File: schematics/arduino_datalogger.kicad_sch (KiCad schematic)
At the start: 9 parts, among them J1 SD card module, J2 RTC module, SW1 SW_Push, U1 DHT22

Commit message: Algunos cambios esquema
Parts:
- added J3: Screw_Terminal_01x03, TerminalBlock:TerminalBlock_bornier-3_P5.08mm, symbol Connector:Screw_Terminal_01x03
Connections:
- net +5V: now also J3.1 (Pin_1)
- net GND: now also J3.3 (Pin_3)
- net DHTDATA: now reaches A1.19 (A0), R3.2, U1.2 (IO)
- net DHTDATA: now also J3.2 (Pin_2)
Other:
- note added: "Not on board"
- moved on the sheet: R3, U1

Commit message: Teniendo en cuenta las medidas reales de los modulos
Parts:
- removed J3: Screw_Terminal_01x03, TerminalBlock:TerminalBlock_bornier-3_P5.08mm, symbol Connector:Screw_Terminal_01x03
- added J3: DHT, Connector_PinSocket_2.54mm:PinSocket_1x06_P2.54mm_Vertical, symbol Connector:Conn_01x03_Socket
- J1, J2: footprint Connector_PinSocket_2.00mm:PinSocket_1x06_P2.00mm_Vertical -> Connector_PinSocket_2.54mm:PinSocket_1x06_P2.54mm_Vertical
- SW1: footprint Button_Switch_THT:SW_PUSH_6mm -> Button_Switch_THT:SW_PUSH-12mm
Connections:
- net +5V: now also J3.1 (Pin_1)
- net DHTDATA: now also J3.2 (Pin_2)
- net GND: now also J3.3 (Pin_3); no longer A1.4 (GND)
- no-connect marks 15 -> 16
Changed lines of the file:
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@@
     (company "Lab. Biología de los Artrópodos - FaCENA - UNNE")
-  )
-  (junction (at 93.98 85.09) (diameter 0) (color 0 0 0 0)
   )
   (junction (at 121.92 54.61) (diameter 0) (color 0 0 0 0)
@@
   (no_connect (at 50.8 57.15))
   (no_connect (at 106.68 53.34))
+  (no_connect (at 93.98 83.82))
   (no_connect (at 81.28 45.72))
   (no_connect (at 50.8 62.23))
@@
     (stroke (width 0) (type default))
   )
-  (wire (pts (xy 93.98 83.82) (xy 93.98 85.09))
-    (stroke (width 0) (type default))
-  )
   (wire (pts (xy 165.1 54.61) (xy 167.64 54.61))
     (stroke (width 0) (type default))
@@
     (stroke (width 0) (type default))
   )
-  (wire (pts (xy 96.52 85.09) (xy 93.98 85.09))
-    (stroke (width 0) (type default))
-  )
   (bus (pts (xy 72.39 60.96) (xy 72.39 63.5))
     (stroke (width 0) (type default))
@@
     (stroke (width 0) (type default))
   )
-  (wire (pts (xy 96.52 83.82) (xy 96.52 85.09))
-    (stroke (width 0) (type default))
-  )
   (wire (pts (xy 34.29 113.03) (xy 43.18 113.03))
     (stroke (width 0) (type default))
@@
   )
   (wire (pts (xy 74.93 34.29) (xy 73.66 34.29))
-    (stroke (width 0) (type default))
-  )
-  (wire (pts (xy 93.98 85.09) (xy 93.98 86.36))
     (stroke (width 0) (type default))
   )
@@
       (effects (font (size 1.27 1.27)) (justify left))
     )
-    (property "Footprint" "Connector_PinSocket_2.00mm:PinSocket_1x06_P2.00mm_Vertical" (at 172.72 46.99 0)
+    (property "Footprint" "Connector_PinSocket_2.54mm:PinSocket_1x06_P2.54mm_Vertical" (at 172.72 46.99 0)
       (effects (font (size 1.27 1.27)) hide)
     )
@@
     )
   )
-  (symbol (lib_id "power:GND") (at 93.98 86.36 0) (unit 1)
-    (in_bom yes) (on_board yes) (dnp no) (fields_autoplaced)
-    (property "Reference" "#PWR02" (at 93.98 92.71 0)
-      (effects (font (size 1.27 1.27)) hide)
-    )
-    (property "Value" "GND" (at 93.98 91.44 0)
-      (effects (font (size 1.27 1.27)))
-    )
-    (property "Footprint" "" (at 93.98 86.36 0)
-      (effects (font (size 1.27 1.27)) hide)
-    )
-    (property "Datasheet" "" (at 93.98 86.36 0)
+  (symbol (lib_id "power:GND") (at 96.52 83.82 0) (unit 1)
+    (in_bom yes) (on_board yes) (dnp no) (fields_autoplaced)
+    (property "Reference" "#PWR02" (at 96.52 90.17 0)
+      (effects (font (size 1.27 1.27)) hide)
+    )
+    (property "Value" "GND" (at 96.52 88.9 0)
+      (effects (font (size 1.27 1.27)))
+    )
+    (property "Footprint" "" (at 96.52 83.82 0)
+      (effects (font (size 1.27 1.27)) hide)
+    )
+    (property "Datasheet" "" (at 96.52 83.82 0)
       (effects (font (size 1.27 1.27)) hide)
     )
@@
     )
   )
-  (symbol (lib_id "Connector:Screw_Terminal_01x03") (at 129.54 58.42 0) (unit 1)
-    (in_bom yes) (on_board yes) (dnp no) (fields_autoplaced)
-    (property "Reference" "J3" (at 132.08 57.15 0)
-      (effects (font (size 1.27 1.27)) (justify left))
-    )
-    (property "Value" "Screw_Terminal_01x03" (at 132.08 59.69 0)
-      (effects (font (size 1.27 1.27)) (justify left))
-    )
-    (property "Footprint" "TerminalBlock:TerminalBlock_bornier-3_P5.08mm" (at 129.54 58.42 0)
+  (symbol (lib_id "Device:R") (at 40.64 33.02 0) (unit 1)
+    (in_bom yes) (on_board yes) (dnp no) (fields_autoplaced)
+    (property "Reference" "R1" (at 43.18 31.75 0)
+      (effects (font (size 1.27 1.27)) (justify left))
+    )
+    (property "Value" "1K" (at 43.18 34.29 0)
+      (effects (font (size 1.27 1.27)) (justify left))
+    )
+    (property "Footprint" "Resistor_THT:R_Axial_DIN0207_L6.3mm_D2.5mm_P7.62mm_Horizontal" (at 38.862 33.02 90)
+      (effects (font (size 1.27 1.27)) hide)
+    )
+    (property "Datasheet" "~" (at 40.64 33.02 0)
+      (effects (font (size 1.27 1.27)) hide)
+    )
+    (pin "1")
+    (pin "2")
+    (instances
+      (project "arduino_datalogger"
+        (path "/b8de69f0-971f-4260-bee1-9a12f00351ec"
+          (reference "R1") (unit 1)
+        )
+      )
+    )
+  )
+  (symbol (lib_id "Connector:Conn_01x03_Socket") (at 129.54 58.42 0) (unit 1)
+    (in_bom yes) (on_board yes) (dnp no) (fields_autoplaced)
+    (property "Reference" "J3" (at 130.81 57.15 0)
+      (effects (font (size 1.27 1.27)) (justify left))
+    )
+    (property "Value" "DHT" (at 130.81 59.69 0)
+      (effects (font (size 1.27 1.27)) (justify left))
+    )
+    (property "Footprint" "Connector_PinSocket_2.54mm:PinSocket_1x06_P2.54mm_Vertical" (at 129.54 58.42 0)
       (effects (font (size 1.27 1.27)) hide)
     )
@@
         (path "/b8de69f0-971f-4260-bee1-9a12f00351ec"
           (reference "J3") (unit 1)
-        )
-      )
-    )
-  )
-  (symbol (lib_id "Device:R") (at 40.64 33.02 0) (unit 1)
-    (in_bom yes) (on_board yes) (dnp no) (fields_autoplaced)
-    (property "Reference" "R1" (at 43.18 31.75 0)
-      (effects (font (size 1.27 1.27)) (justify left))
-    )
-    (property "Value" "1K" (at 43.18 34.29 0)
-      (effects (font (size 1.27 1.27)) (justify left))
-    )
-    (property "Footprint" "Resistor_THT:R_Axial_DIN0207_L6.3mm_D2.5mm_P7.62mm_Horizontal" (at 38.862 33.02 90)
-      (effects (font (size 1.27 1.27)) hide)
-    )
-    (property "Datasheet" "~" (at 40.64 33.02 0)
-      (effects (font (size 1.27 1.27)) hide)
-    )
-    (pin "1")
-    (pin "2")
-    (instances
-      (project "arduino_datalogger"
-        (path "/b8de69f0-971f-4260-bee1-9a12f00351ec"
-          (reference "R1") (unit 1)
         )
       )
@@
       (effects (font (size 1.27 1.27)))
     )
-    (property "Footprint" "Button_Switch_THT:SW_PUSH_6mm" (at 68.58 29.21 0)
+    (property "Footprint" "Button_Switch_THT:SW_PUSH-12mm" (at 68.58 29.21 0)
       (effects (font (size 1.27 1.27)) hide)
     )
@@
       (effects (font (size 1.27 1.27)) (justify left))
     )
-    (property "Footprint" "Connector_PinSocket_2.00mm:PinSocket_1x06_P2.00mm_Vertical" (at 172.72 66.04 0)
-      (effects (font (size 1.27 1.27)) hide)
-    )
+    (property "Footprint" "Connector_PinSocket_2.54mm:PinSocket_1x06_P2.54mm_Vertical" (at 172.72 66.04 0)
+      (effects (font (size 1.27 1.27)) hide)
+    )

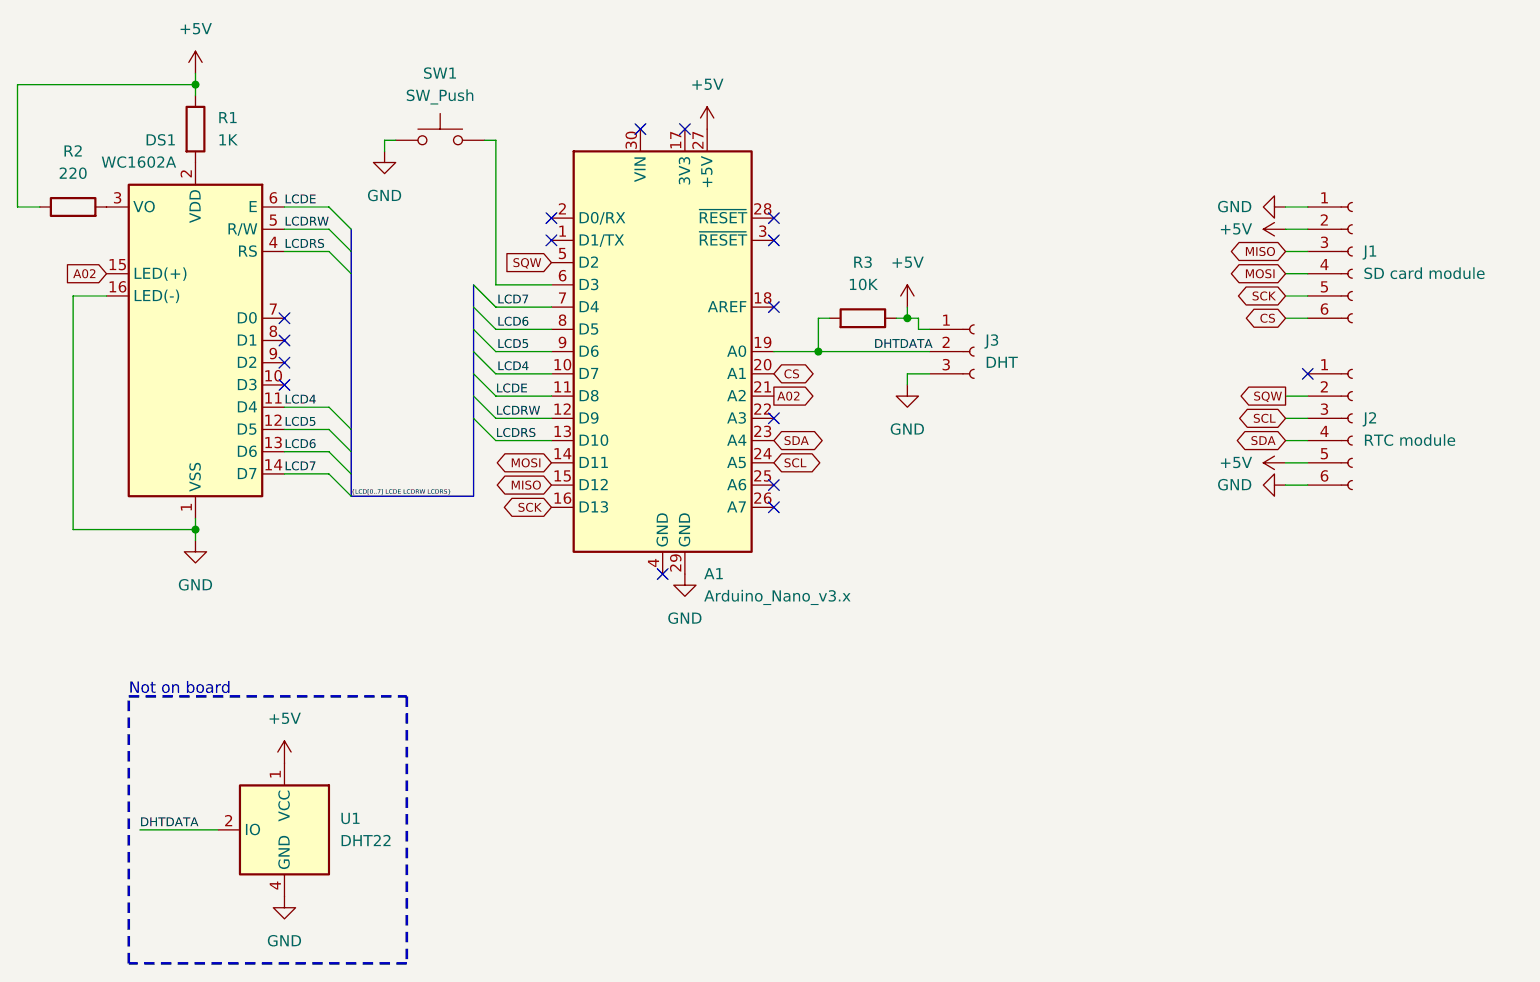
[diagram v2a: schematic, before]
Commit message: Simbolos y footprints para modulo RTC y microSD
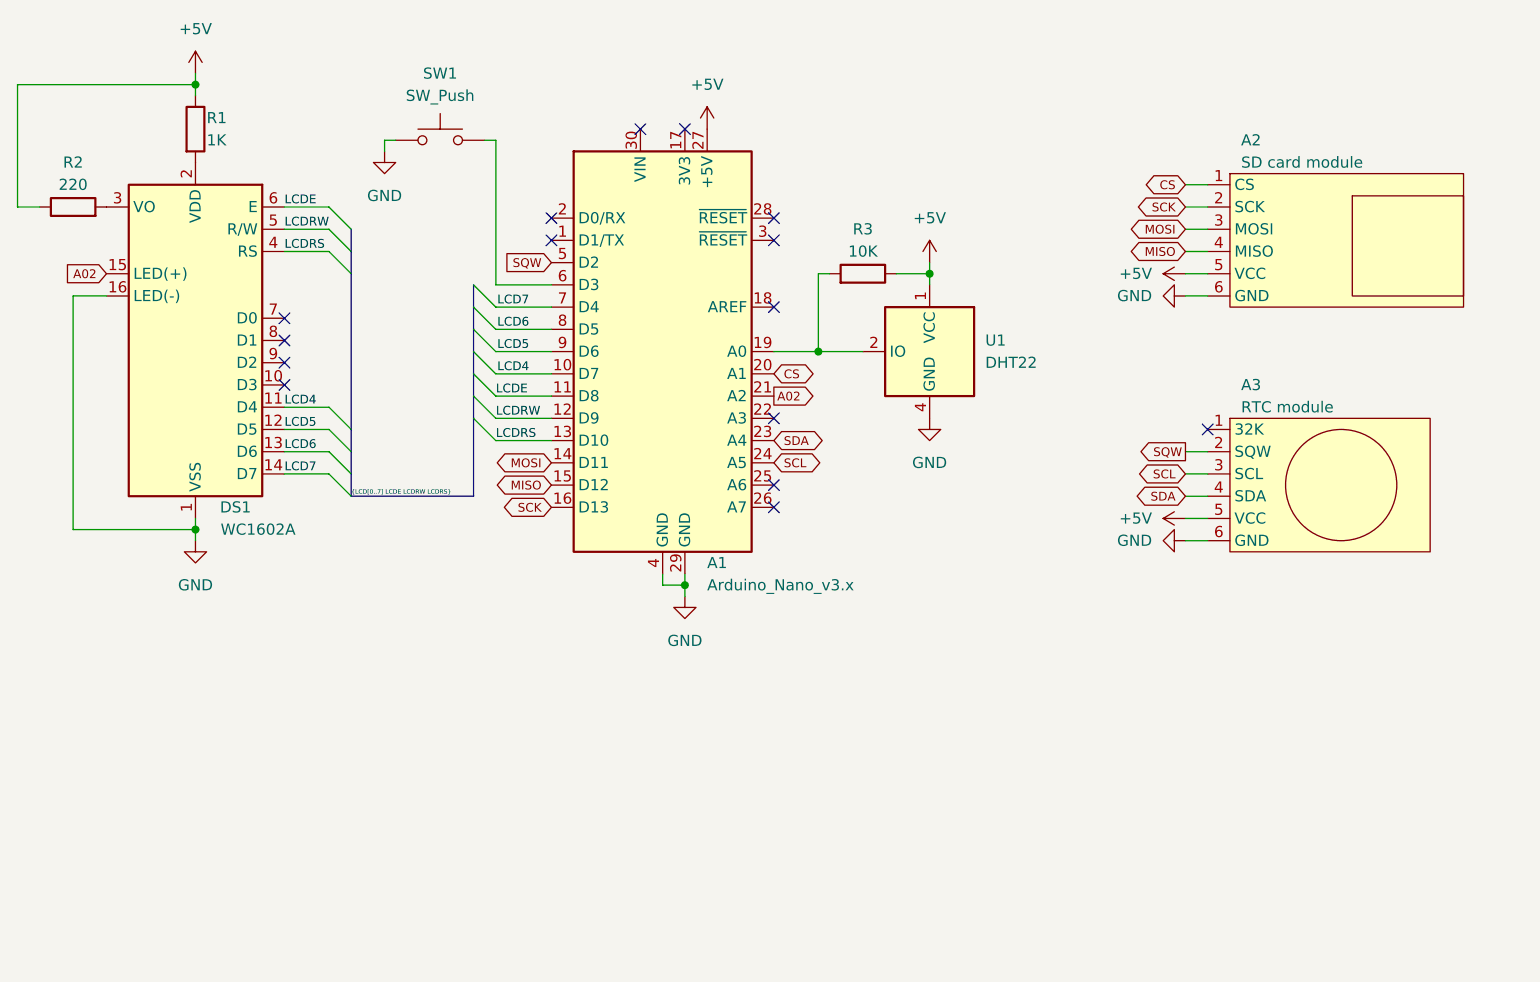
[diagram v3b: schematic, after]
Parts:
- removed J3: DHT, Connector_PinSocket_2.54mm:PinSocket_1x06_P2.54mm_Vertical, symbol Connector:Conn_01x03_Socket
- A2: renamed from J1; footprint Connector_PinSocket_2.54mm:PinSocket_1x06_P2.54mm_Vertical -> Custom_Modules:MicroSD_Module; symbol Connector:Conn_01x06_Socket -> Custom_Modules:MicroSD_Module
- A3: renamed from J2; footprint Connector_PinSocket_2.54mm:PinSocket_1x06_P2.54mm_Vertical -> Custom_Modules:RTCDS3231; symbol Connector:Conn_01x06_Socket -> Custom_Modules:RTCDS3231
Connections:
- net +5V: now also A2.5 (VCC); no longer A2.2 (Pin_2)
- net CS: now also A2.1 (CS); no longer A2.6 (Pin_6)
- net GND: now also A1.4 (GND), A2.6 (GND); no longer A2.1 (Pin_1)
- net MISO: now also A2.4 (MISO); no longer A2.3 (Pin_3)
- net MOSI: now also A2.3 (MOSI); no longer A2.4 (Pin_4)
- net SCK: now also A2.2 (SCK); no longer A2.5 (Pin_5)
- net DHTDATA: no longer names the net of A1.19 (A0), R3.2, U1.2 (IO)
- no-connect marks 16 -> 15
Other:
- note removed: "Not on board"
- moved on the sheet: R3, U1
